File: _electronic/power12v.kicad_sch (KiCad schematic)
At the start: 16 parts

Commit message: organized electronics folder
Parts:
- JP1, JP2: # (none) -> xxx; Mouser (none) -> OK
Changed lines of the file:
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@@
+      (effects (font (size 1.27 1.27)) hide)
+    )
+    (property "#" "xxx" (id 4) (at 146.05 66.04 0)
+      (effects (font (size 1.27 1.27)) hide)
+    )
+    (property "Mouser" "OK" (id 5) (at 146.05 66.04 0)
       (effects (font (size 1.27 1.27)) hide)
     )
@@
       (effects (font (size 1.27 1.27)) hide)
     )
+    (property "#" "xxx" (id 4) (at 146.05 73.66 0)
+      (effects (font (size 1.27 1.27)) hide)
+    )
+    (property "Mouser" "OK" (id 5) (at 146.05 73.66 0)
+      (effects (font (size 1.27 1.27)) hide)
+    )

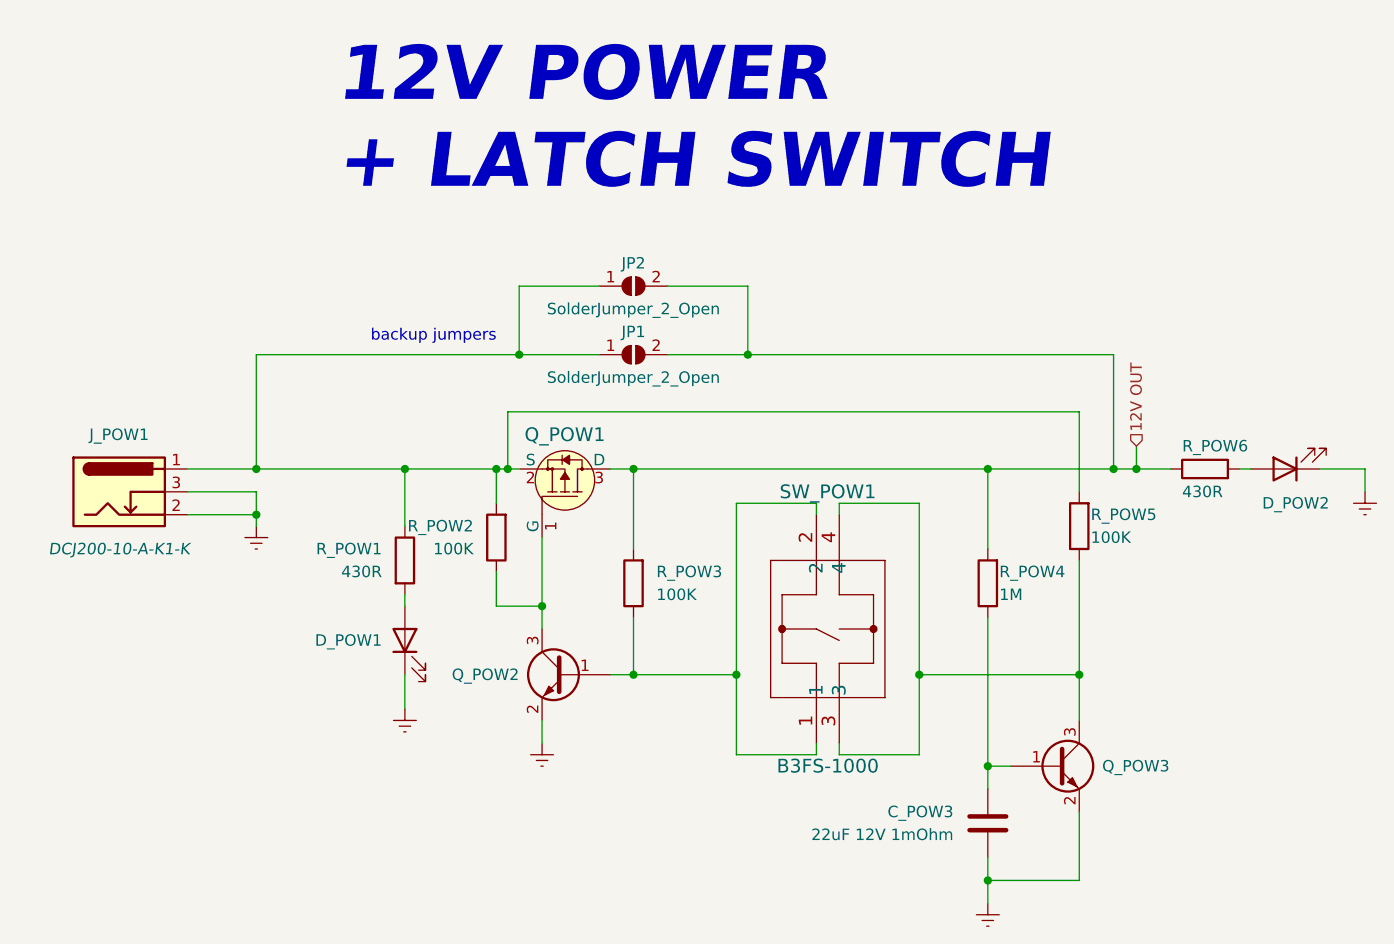
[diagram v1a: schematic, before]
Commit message: revised pcb: direct power, leds, ftdi w/o 3v3
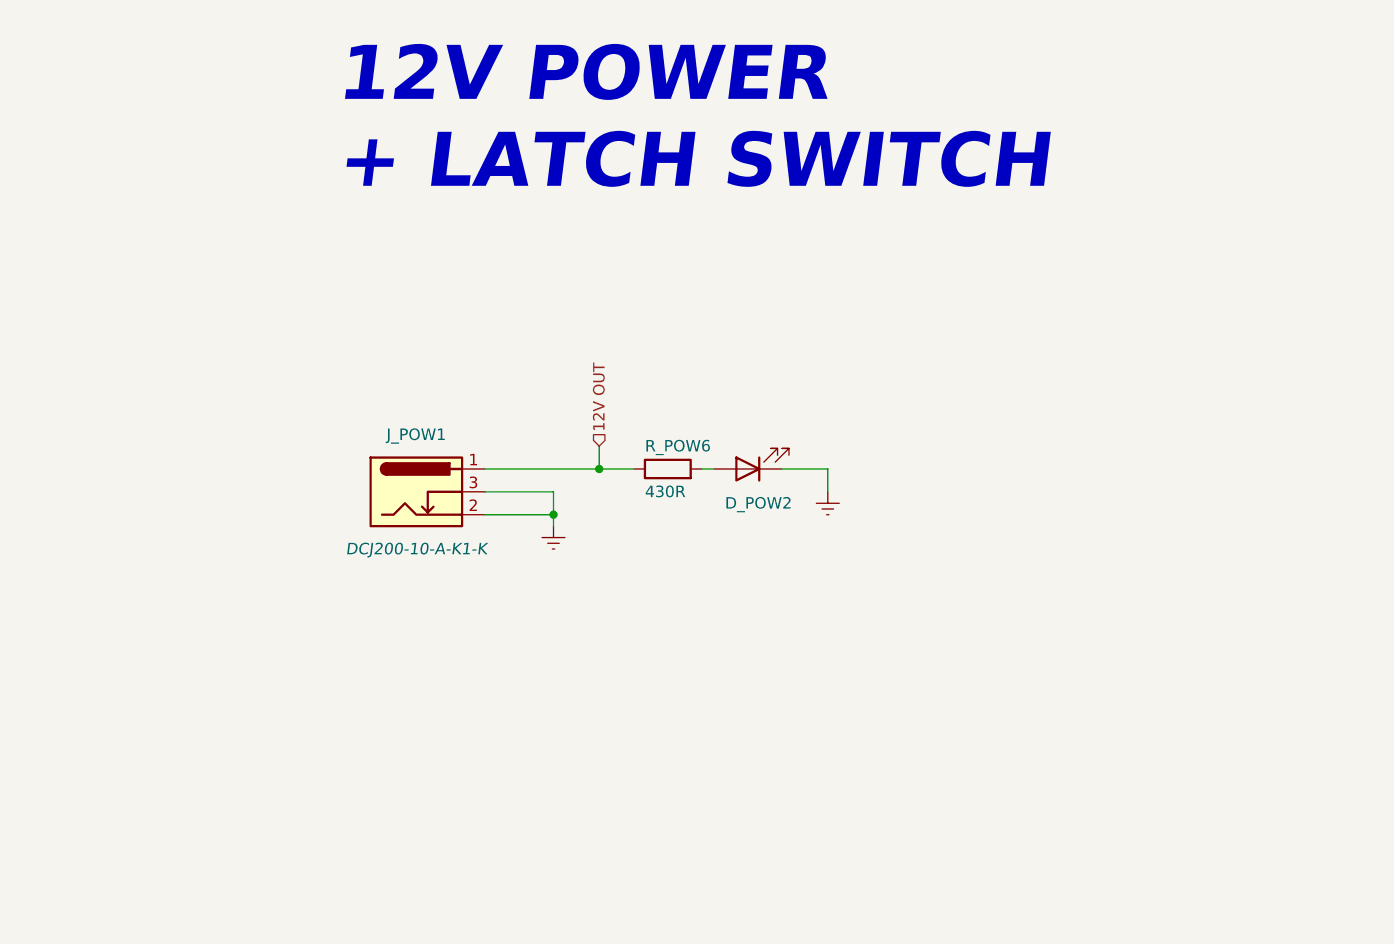
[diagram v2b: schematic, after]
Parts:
- removed C_POW3: 22uF 12V 1mOhm, Capacitor_SMD:C_0603_1608Metric_Pad1.08x0.95mm_HandSolder, symbol Device:C
- removed D_POW1: LED white, LED_SMD:LED_0603_1608Metric_Pad1.05x0.95mm_HandSolder, symbol Device:LED
- removed JP1, JP2: SolderJumper_2_Open, Jumper:SolderJumper-2_P1.3mm_Open_Pad1.0x1.5mm, symbol Jumper:SolderJumper_2_Open
- removed Q_POW1: SQ2351ES-T1_GE3, Package_TO_SOT_SMD:SOT-23_Handsoldering, symbol dk_Transistors-FETs-MOSFETs-Single:AO3401A
- removed Q_POW2, Q_POW3: MMBT3904,215, Package_TO_SOT_SMD:SOT-23_Handsoldering, symbol Transistor_BJT:2SC4213
- removed R_POW1: 430R, Resistor_SMD:R_0603_1608Metric_Pad0.98x0.95mm_HandSolder, symbol Device:R
- removed R_POW2, R_POW3, R_POW5: 100K, Resistor_SMD:R_0603_1608Metric_Pad0.98x0.95mm_HandSolder, symbol Device:R
- removed R_POW4: 1M, Resistor_SMD:R_0603_1608Metric_Pad0.98x0.95mm_HandSolder, symbol Device:R
- removed SW_POW1: B3FS-1000, b3fs:B3FS-1000, symbol 2022-07-12_23-59-33:B3FS-1000
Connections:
- net 12V OUT: now also J_POW1.1
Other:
- note removed: "backup jumpers"
- moved on the sheet: D_POW2, J_POW1, R_POW6

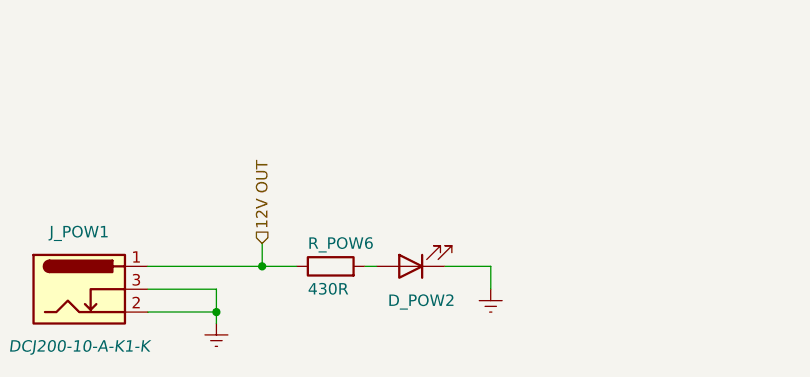
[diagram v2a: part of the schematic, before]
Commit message: led resistor revision, b.o.m. and pcb anotation
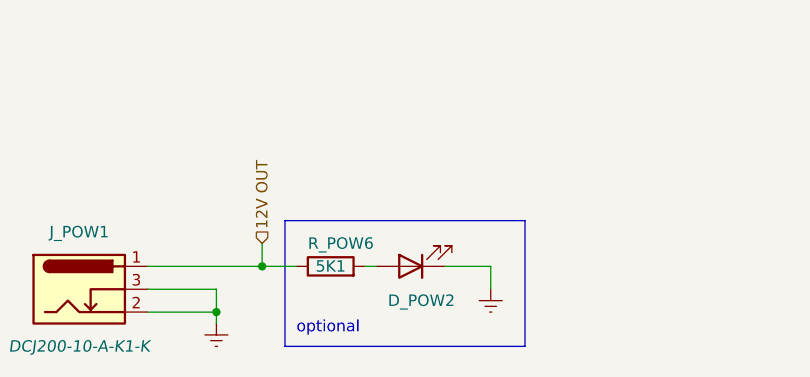
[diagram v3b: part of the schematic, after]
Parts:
- R_POW6: value 430R -> 5K1; # CR0603-JW-431ELF -> ERJ-3EKF5101V
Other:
- note added: "optional"
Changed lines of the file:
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@@
+    (stroke (width 0) (type default) (color 0 0 0 0))
+  )
+  (polyline (pts (xy 144.78 81.28) (xy 171.45 81.28))
     (stroke (width 0) (type default) (color 0 0 0 0))
   )
@@
   )
   (wire (pts (xy 154.94 86.36) (xy 153.67 86.36))
+    (stroke (width 0) (type default) (color 0 0 0 0))
+  )
+  (polyline (pts (xy 171.45 95.25) (xy 144.78 95.25))
+    (stroke (width 0) (type default) (color 0 0 0 0))
+  )
+  (polyline (pts (xy 144.78 81.28) (xy 144.78 95.25))
     (stroke (width 0) (type default) (color 0 0 0 0))
   )
@@
   (wire (pts (xy 137.16 91.44) (xy 137.16 92.71))
     (stroke (width 0) (type default) (color 0 0 0 0))
+  )
+  (polyline (pts (xy 171.45 81.28) (xy 171.45 95.25))
+    (stroke (width 0) (type default) (color 0 0 0 0))
+  )
+  (text "optional" (at 146.05 93.98 0)
+    (effects (font (size 1.27 1.27)) (justify left bottom))
   )
   (text "12V POWER\n+ LATCH SWITCH" (at 113.03 55.88 0)
@@
       (effects (font (size 1.27 1.27)) (justify right))
     )
-    (property "Value" "430R" (id 1) (at 147.32 88.9 90)
-      (effects (font (size 1.27 1.27)) (justify right))
-    )
+    (property "Value" "5K1" (id 1) (at 149.86 86.36 90))
     (property "Footprint" "Resistor_SMD:R_0603_1608Metric_Pad0.98x0.95mm_HandSolder" (id 2) (at 149.86 88.138 90)
       (effects (font (size 1.27 1.27)) hide)
@@
       (effects (font (size 1.27 1.27)) hide)
     )
-    (property "#" "CR0603-JW-431ELF" (id 4) (at 151.13 83.82 0)
+    (property "#" "ERJ-3EKF5101V" (id 4) (at 151.13 83.82 0)
       (effects (font (size 1.27 1.27) italic) (justify left) hide)
     )

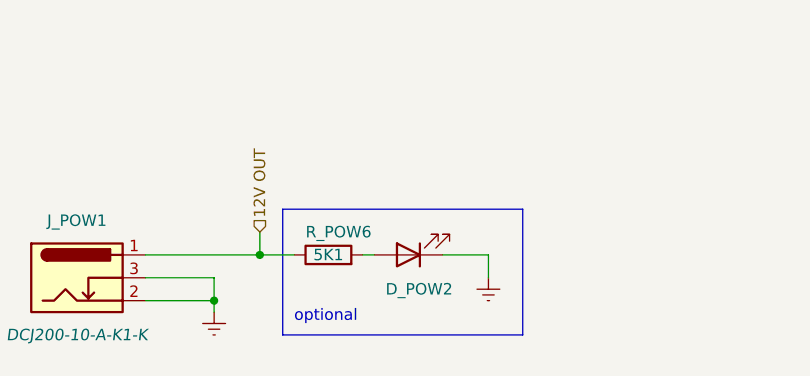
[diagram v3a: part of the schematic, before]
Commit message: schematics and pcb cleanup
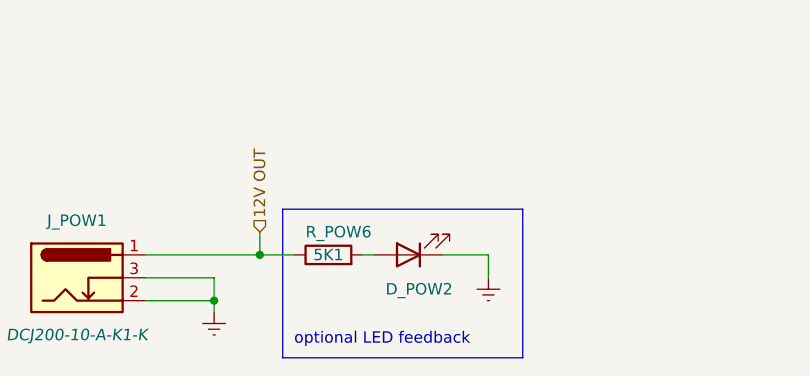
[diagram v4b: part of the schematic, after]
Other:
- note added: "optional LED feedback"
- note removed: "optional"
- title: E-TKT -> E-TKT v1.0
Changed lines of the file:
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@@
   (paper "A4")
   (title_block
-    (title "E-TKT")
-    (date "2022-07-21")
-    (rev "3")
+    (title "E-TKT v1.0")
+    (date "2022-09-29")
+    (rev "4")
     (company "Andrei Speridiao")
   )
@@
     (stroke (width 0) (type default) (color 0 0 0 0))
   )
-  (polyline (pts (xy 171.45 95.25) (xy 144.78 95.25))
+  (polyline (pts (xy 171.45 97.79) (xy 144.78 97.79))
     (stroke (width 0) (type default) (color 0 0 0 0))
   )
-  (polyline (pts (xy 144.78 81.28) (xy 144.78 95.25))
+  (polyline (pts (xy 144.78 81.28) (xy 144.78 97.79))
     (stroke (width 0) (type default) (color 0 0 0 0))
   )
@@
     (stroke (width 0) (type default) (color 0 0 0 0))
   )
-  (polyline (pts (xy 171.45 81.28) (xy 171.45 95.25))
+  (polyline (pts (xy 171.45 81.28) (xy 171.45 97.79))
     (stroke (width 0) (type default) (color 0 0 0 0))
   )
-  (text "optional" (at 146.05 93.98 0)
+  (text "optional LED feedback" (at 146.05 96.52 0)
     (effects (font (size 1.27 1.27)) (justify left bottom))
   )
